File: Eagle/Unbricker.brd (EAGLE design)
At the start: 133.3 x 36.8 mm, 7 parts, among them Q1 2N3906

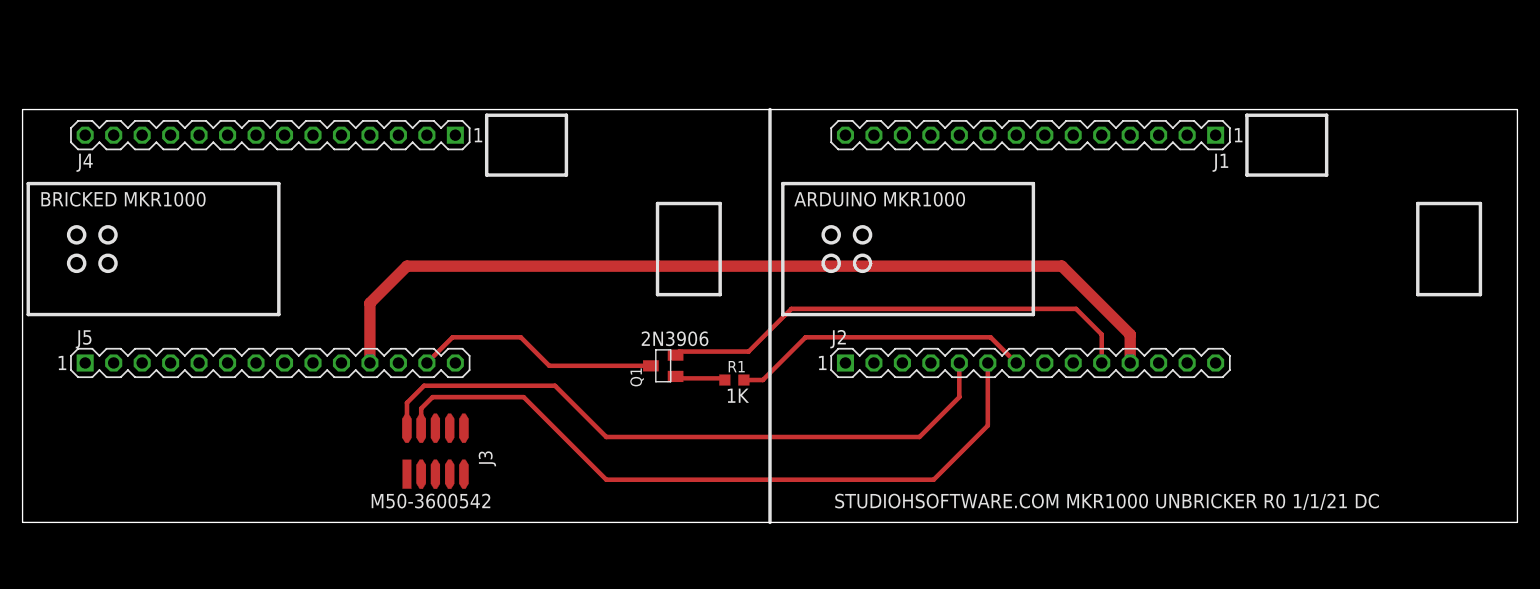
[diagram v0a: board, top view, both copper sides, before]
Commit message: Fix power line, add standoffs, etc.
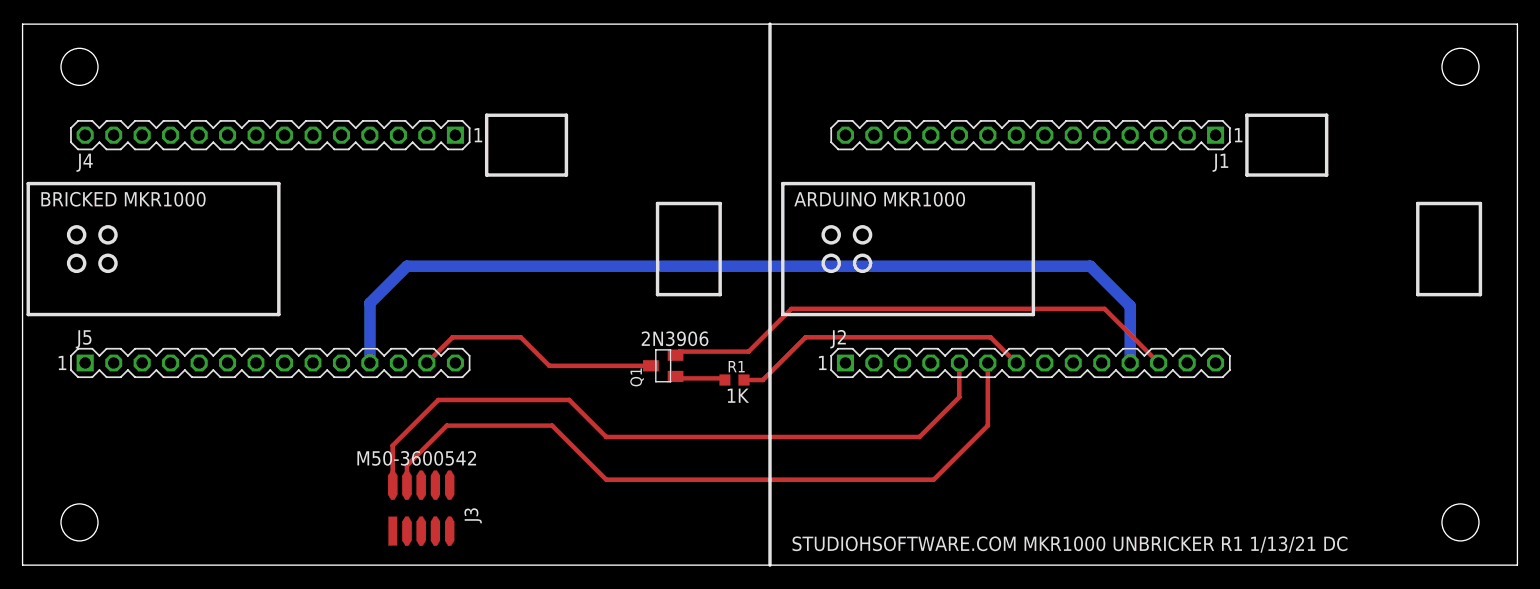
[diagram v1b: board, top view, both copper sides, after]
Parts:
- moved J3 5.24 mm to (35.6, 1.27)
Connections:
- net VCC: now also J2.12; no longer J2.10
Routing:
- net VCC: track 43.2 -> 46.8 mm
- net D10_SWDIO: track 58.6 -> 61.7 mm
- net GND: track 79.6 -> 81.1 mm
- net D11_SWCLK: track 63.4 -> 64.6 mm
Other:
- board size 133.3 x 36.8 mm -> 133.3 x 48.3 mm
- board text added: "STUDIOHSOFTWARE.COM MKR1000 UNBRICKER R1 1/13/21 DC"
- board text removed: "STUDIOHSOFTWARE.COM MKR1000 UNBRICKER R0 1/1/21 DC"
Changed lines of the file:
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@@
 <board>
 <plain>
-<wire x1="133.35" y1="36.83" x2="0" y2="36.83" width="0.0254" layer="20"/>
-<wire x1="133.35" y1="0" x2="0" y2="0" width="0.0254" layer="20"/>
-<wire x1="133.35" y1="36.83" x2="133.35" y2="0" width="0.0254" layer="20"/>
-<wire x1="0" y1="36.83" x2="0" y2="0" width="0.0254" layer="20"/>
-<text x="72.39" y="1.27" size="1.27" layer="25" font="vector" ratio="12">STUDIOHSOFTWARE.COM MKR1000 UNBRICKER R0 1/1/21 DC</text>
+<wire x1="133.35" y1="44.45" x2="0" y2="44.45" width="0.0254" layer="20"/>
+<wire x1="133.35" y1="-3.81" x2="0" y2="-3.81" width="0.0254" layer="20"/>
+<wire x1="133.35" y1="44.45" x2="133.35" y2="-3.81" width="0.0254" layer="20"/>
+<wire x1="0" y1="44.45" x2="0" y2="-3.81" width="0.0254" layer="20"/>
+<text x="68.58" y="-2.54" size="1.27" layer="25" font="vector" ratio="12">STUDIOHSOFTWARE.COM MKR1000 UNBRICKER R1 1/13/21 DC</text>
 <text x="1.524" y="28.194" size="1.27" layer="25" font="vector" ratio="12">BRICKED MKR1000</text>
 <circle x="4.826" y="25.654" radius="0.71841875" width="0.3048" layer="21"/>
@@
 <wire x1="48.514" y1="30.988" x2="48.514" y2="36.322" width="0.3048" layer="21"/>
 <wire x1="48.514" y1="36.322" x2="41.402" y2="36.322" width="0.3048" layer="21"/>
-<wire x1="66.675" y1="0" x2="66.675" y2="36.83" width="0.3048" layer="21"/>
+<wire x1="66.675" y1="-3.81" x2="66.675" y2="44.45" width="0.3048" layer="21"/>
 <text x="68.834" y="28.194" size="1.27" layer="25" font="vector" ratio="12">ARDUINO MKR1000</text>
 <circle x="72.136" y="25.654" radius="0.71841875" width="0.3048" layer="21"/>
@@
 <text x="55.118" y="15.748" size="1.27" layer="25" font="vector" ratio="12">2N3906</text>
 <text x="62.738" y="10.668" size="1.27" layer="25" font="vector" ratio="12">1K</text>
-<text x="30.988" y="1.27" size="1.27" layer="25" font="vector" ratio="12">M50-3600542</text>
+<text x="29.718" y="5.08" size="1.27" layer="25" font="vector" ratio="12">M50-3600542</text>
+<hole x="128.27" y="40.64" drill="3.302"/>
+<hole x="128.27" y="0" drill="3.302"/>
+<hole x="5.08" y="0" drill="3.302"/>
+<hole x="5.08" y="40.64" drill="3.302"/>
 </plain>
 <attributes>
@@
 <attribute name="Z_SMT" value="Y" x="63.5" y="12.7" size="1.778" layer="27" display="off"/>
 </element>
-<element name="J3" library="MK1_Zero" package="FCI-MINITEK127HDR-10" value="" x="36.83" y="6.35" smashed="yes" rot="R90">
-<attribute name="MF" value="Harwin" x="36.83" y="6.35" size="1.778" layer="27" rot="R90" display="off"/>
-<attribute name="DESCR" value="STRIP 1.27MM VERT SMD 5x2POS " x="36.83" y="6.35" size="1.778" layer="27" rot="R90" display="off"/>
-<attribute name="MPN" value="M50-3600542 " x="36.83" y="6.35" size="1.778" layer="27" rot="R90" display="off"/>
-<attribute name="NAME" x="41.91" y="5.08" size="1.2" layer="25" font="vector" ratio="10" rot="R90"/>
-<attribute name="VALUE" x="36.83" y="6.35" size="1.2" layer="27" font="vector" ratio="10" rot="R90"/>
+<element name="J3" library="MK1_Zero" package="FCI-MINITEK127HDR-10" value="" x="35.56" y="1.27" smashed="yes" rot="R90">
+<attribute name="MF" value="Harwin" x="35.56" y="1.27" size="1.778" layer="27" rot="R90" display="off"/>
+<attribute name="DESCR" value="STRIP 1.27MM VERT SMD 5x2POS " x="35.56" y="1.27" size="1.778" layer="27" rot="R90" display="off"/>
+<attribute name="MPN" value="M50-3600542 " x="35.56" y="1.27" size="1.778" layer="27" rot="R90" display="off"/>
+<attribute name="NAME" x="40.64" y="0" size="1.2" layer="25" font="vector" ratio="10" rot="R90"/>
+<attribute name="VALUE" x="35.56" y="1.27" size="1.2" layer="27" font="vector" ratio="10" rot="R90"/>
 </element>
 </elements>
@@
 <contactref element="J5" pad="11"/>
 <contactref element="J2" pad="11"/>
-<wire x1="30.988" y1="14.224" x2="30.988" y2="19.558" width="1.016" layer="1"/>
-<wire x1="30.988" y1="19.558" x2="34.29" y2="22.86" width="1.016" layer="1"/>
-<wire x1="34.29" y1="22.86" x2="92.71" y2="22.86" width="1.016" layer="1"/>
-<wire x1="92.71" y1="22.86" x2="98.806" y2="16.764" width="1.016" layer="1"/>
-<wire x1="98.806" y1="14.224" x2="98.806" y2="16.764" width="1.016" layer="1"/>
+<wire x1="30.988" y1="14.224" x2="30.988" y2="19.558" width="1.016" layer="16"/>
+<wire x1="30.988" y1="19.558" x2="34.29" y2="22.86" width="1.016" layer="16"/>
+<wire x1="34.29" y1="22.86" x2="95.25" y2="22.86" width="1.016" layer="16"/>
+<wire x1="95.25" y1="22.86" x2="98.806" y2="19.304" width="1.016" layer="16"/>
+<wire x1="98.806" y1="14.224" x2="98.806" y2="19.304" width="1.016" layer="16"/>
 </signal>
 <signal name="VCC">
-<contactref element="J2" pad="10"/>
 <contactref element="Q1" pad="3"/>
 <wire x1="64.77" y1="15.24" x2="58.57" y2="15.24" width="0.4064" layer="1"/>
 <wire x1="58.57" y1="15.24" x2="58.25" y2="14.92" width="0.4064" layer="1"/>
 <wire x1="64.77" y1="15.24" x2="68.58" y2="19.05" width="0.4064" layer="1"/>
-<wire x1="68.58" y1="19.05" x2="93.98" y2="19.05" width="0.4064" layer="1"/>
-<wire x1="96.266" y1="14.224" x2="96.266" y2="16.764" width="0.4064" layer="1"/>
-<wire x1="96.266" y1="16.764" x2="93.98" y2="19.05" width="0.4064" layer="1"/>
+<wire x1="68.58" y1="19.05" x2="96.52" y2="19.05" width="0.4064" layer="1"/>
+<contactref element="J2" pad="12"/>
+<wire x1="96.52" y1="19.05" x2="101.346" y2="14.224" width="0.4064" layer="1"/>
 </signal>
 <signal name="D12">
@@
 <contactref element="J3" pad="2"/>
 <contactref element="J2" pad="5"/>
-<wire x1="34.29" y1="8.4" x2="34.29" y2="10.668" width="0.4064" layer="1"/>
-<wire x1="34.29" y1="10.668" x2="35.814" y2="12.192" width="0.4064" layer="1"/>
-<wire x1="35.814" y1="12.192" x2="47.498" y2="12.192" width="0.4064" layer="1"/>
-<wire x1="47.498" y1="12.192" x2="52.07" y2="7.62" width="0.4064" layer="1"/>
+<wire x1="33.02" y1="3.32" x2="33.02" y2="6.858" width="0.4064" layer="1"/>
+<wire x1="33.02" y1="6.858" x2="37.084" y2="10.922" width="0.4064" layer="1"/>
+<wire x1="37.084" y1="10.922" x2="48.768" y2="10.922" width="0.4064" layer="1"/>
+<wire x1="48.768" y1="10.922" x2="52.07" y2="7.62" width="0.4064" layer="1"/>
 <wire x1="52.07" y1="7.62" x2="80.01" y2="7.62" width="0.4064" layer="1"/>
 <wire x1="83.566" y1="14.224" x2="83.566" y2="11.176" width="0.4064" layer="1"/>
@@
 <contactref element="J2" pad="6"/>
 <wire x1="52.07" y1="3.81" x2="81.28" y2="3.81" width="0.4064" layer="1"/>
-<wire x1="35.56" y1="8.4" x2="35.56" y2="10.16" width="0.4064" layer="1"/>
-<wire x1="35.56" y1="10.16" x2="36.576" y2="11.176" width="0.4064" layer="1"/>
-<wire x1="36.576" y1="11.176" x2="44.704" y2="11.176" width="0.4064" layer="1"/>
-<wire x1="44.704" y1="11.176" x2="52.07" y2="3.81" width="0.4064" layer="1"/>
+<wire x1="34.29" y1="3.32" x2="34.29" y2="5.08" width="0.4064" layer="1"/>
+<wire x1="34.29" y1="5.08" x2="37.846" y2="8.636" width="0.4064" layer="1"/>
+<wire x1="37.846" y1="8.636" x2="47.244" y2="8.636" width="0.4064" layer="1"/>
+<wire x1="47.244" y1="8.636" x2="52.07" y2="3.81" width="0.4064" layer="1"/>
 <wire x1="86.106" y1="14.224" x2="86.106" y2="8.636" width="0.4064" layer="1"/>
 <wire x1="86.106" y1="8.636" x2="81.28" y2="3.81" width="0.4064" layer="1"/>
